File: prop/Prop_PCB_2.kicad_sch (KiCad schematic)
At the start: 42 parts

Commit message: finalize3pcb schematic
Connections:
- net CS is gone; now on net CS1: U?.10 (~{CS}/SHDN)
- net aData0: now also J?.3
- net aData1: now also J?.3
- net aData2: now also J?.3
- net aData3: now also J?.3
- net aData4: now also J?.3
- no-connect marks 31 -> 38

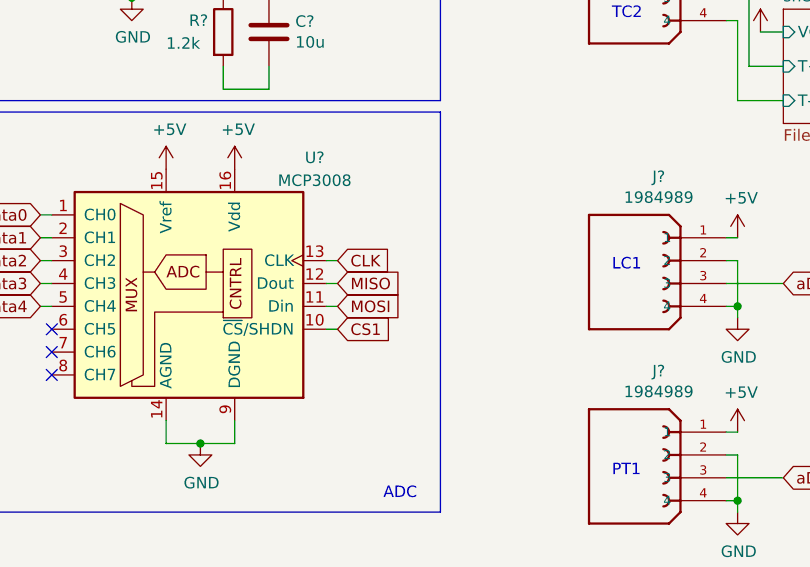
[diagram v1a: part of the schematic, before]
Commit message: fix spelling errors in signals
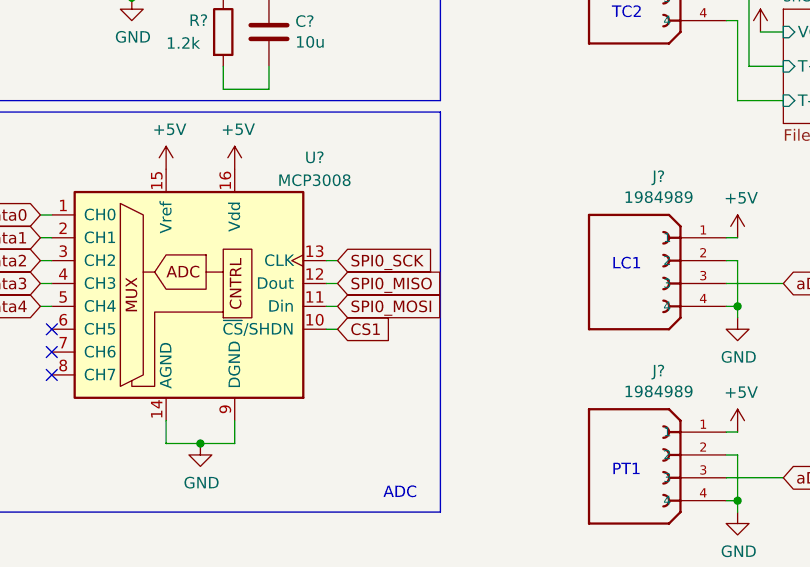
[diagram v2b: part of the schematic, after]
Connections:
- net CLK is gone; now on net SPI0_SCK: U?.13 (CLK)
- net MISO is gone; now on net SPI0_MISO: U?.12 (Dout)
- net MOSI is gone; now on net SPI0_MOSI: U?.11 (Din)
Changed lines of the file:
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@@
     (effects (font (size 1.27 1.27)) (justify left bottom))
   )
-  (global_label "MISO" (shape input) (at 113.03 74.93 0) (fields_autoplaced)
+  (global_label "SPI0_MISO" (shape input) (at 113.03 74.93 0) (fields_autoplaced)
     (effects (font (size 1.27 1.27)) (justify left))
-    (property "Intersheet References" "${INTERSHEET_REFS}" (id 0) (at 120.0393 74.8506 0)
+    (property "Intersheet References" "${INTERSHEET_REFS}" (id 0) (at 125.3007 74.8506 0)
       (effects (font (size 1.27 1.27)) (justify left) hide)
     )
@@
     )
   )
-  (global_label "CLK" (shape input) (at 113.03 72.39 0) (fields_autoplaced)
+  (global_label "SPI0_SCK" (shape input) (at 113.03 72.39 0) (fields_autoplaced)
     (effects (font (size 1.27 1.27)) (justify left))
-    (property "Intersheet References" "${INTERSHEET_REFS}" (id 0) (at 119.0112 72.3106 0)
+    (property "Intersheet References" "${INTERSHEET_REFS}" (id 0) (at 124.4541 72.3106 0)
       (effects (font (size 1.27 1.27)) (justify left) hide)
     )
@@
     )
   )
-  (global_label "MOSI" (shape input) (at 113.03 77.47 0) (fields_autoplaced)
+  (global_label "SPI0_MOSI" (shape input) (at 113.03 77.47 0) (fields_autoplaced)
     (effects (font (size 1.27 1.27)) (justify left))
-    (property "Intersheet References" "${INTERSHEET_REFS}" (id 0) (at 120.0393 77.3906 0)
+    (property "Intersheet References" "${INTERSHEET_REFS}" (id 0) (at 125.3007 77.3906 0)
       (effects (font (size 1.27 1.27)) (justify left) hide)
     )
@@
       (reference "#PWR?") (unit 1) (value "GND") (footprint "")
     )
+    (path "/49575217-40b0-4890-8acf-12982cca52b5/00000000-0000-0000-0000-000060597f92"
+      (reference "#PWR?") (unit 1) (value "GND") (footprint "")
+    )
     (path "/7db990e4-92e1-4f99-b4d2-435bbec1ba83/00000000-0000-0000-0000-000060597f92"
-      (reference "#PWR?") (unit 1) (value "GND") (footprint "")
-    )
-    (path "/49575217-40b0-4890-8acf-12982cca52b5/00000000-0000-0000-0000-000060597f92"
       (reference "#PWR?") (unit 1) (value "GND") (footprint "")
     )
@@
       (reference "U?") (unit 1) (value "MCP3008") (footprint "Package_SO:SOIC-16_3.9x9.9mm_P1.27mm")
     )
+    (path "/49575217-40b0-4890-8acf-12982cca52b5/65a8b55e-a85b-43de-a7c0-277e3d0e143e"
+      (reference "U?") (unit 1) (value "MAX6675ISA+") (footprint "star-common-lib:SOIC127P600X175-8N")
+    )
     (path "/7db990e4-92e1-4f99-b4d2-435bbec1ba83/65a8b55e-a85b-43de-a7c0-277e3d0e143e"
       (reference "U?") (unit 1) (value "MAX6675ISA+") (footprint "star-common-lib:SOIC127P600X175-8N")
     )
-    (path "/49575217-40b0-4890-8acf-12982cca52b5/65a8b55e-a85b-43de-a7c0-277e3d0e143e"
-      (reference "U?") (unit 1) (value "MAX6675ISA+") (footprint "star-common-lib:SOIC127P600X175-8N")
-    )

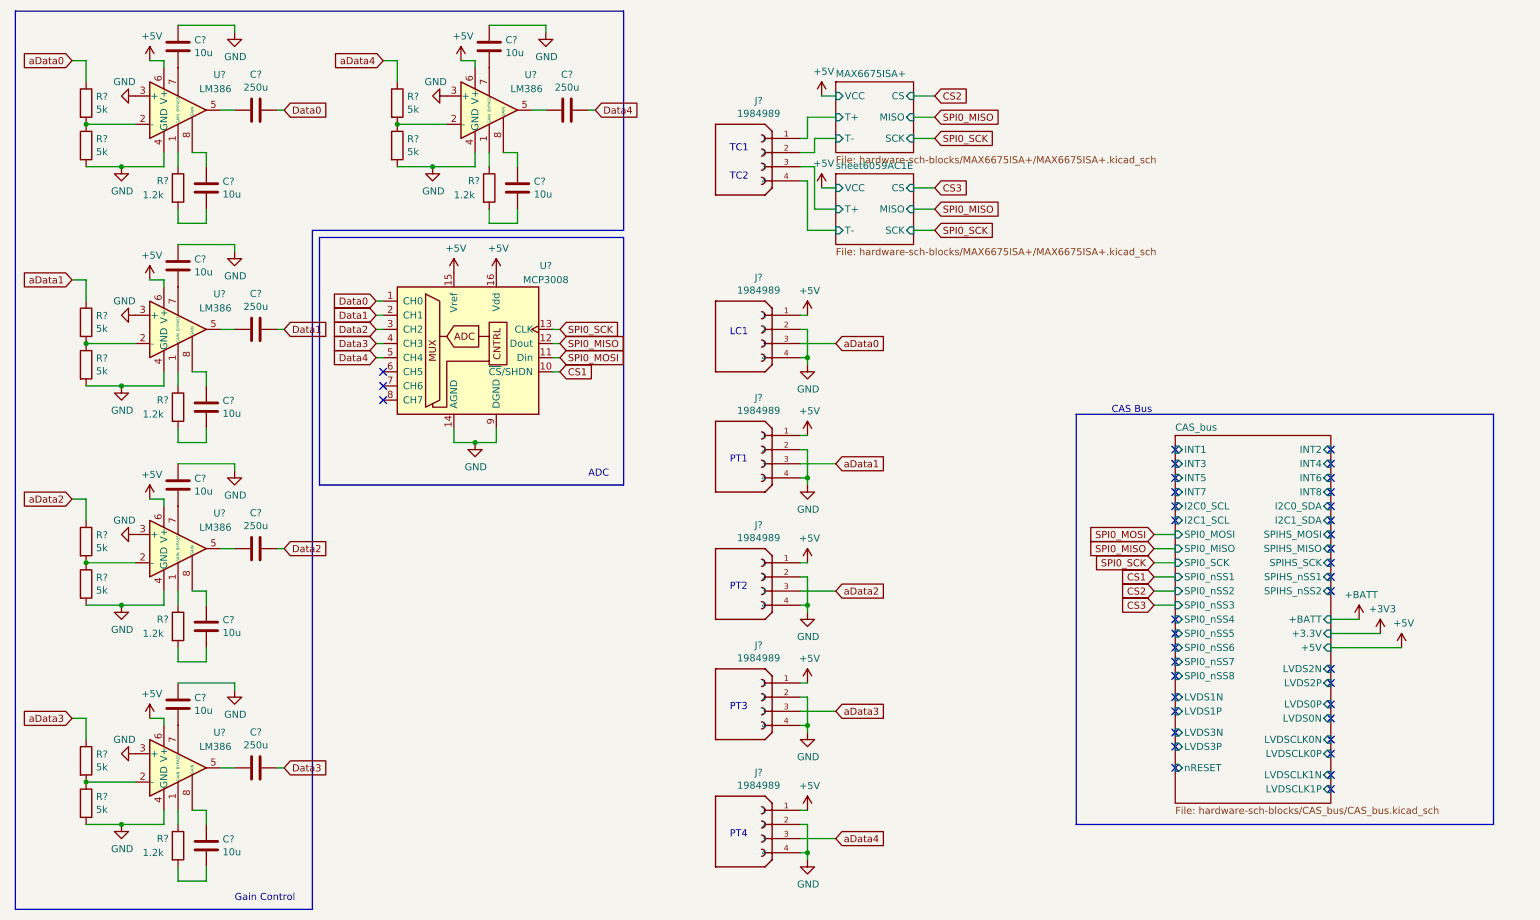
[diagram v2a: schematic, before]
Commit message: rearranged the pcb to be more neat
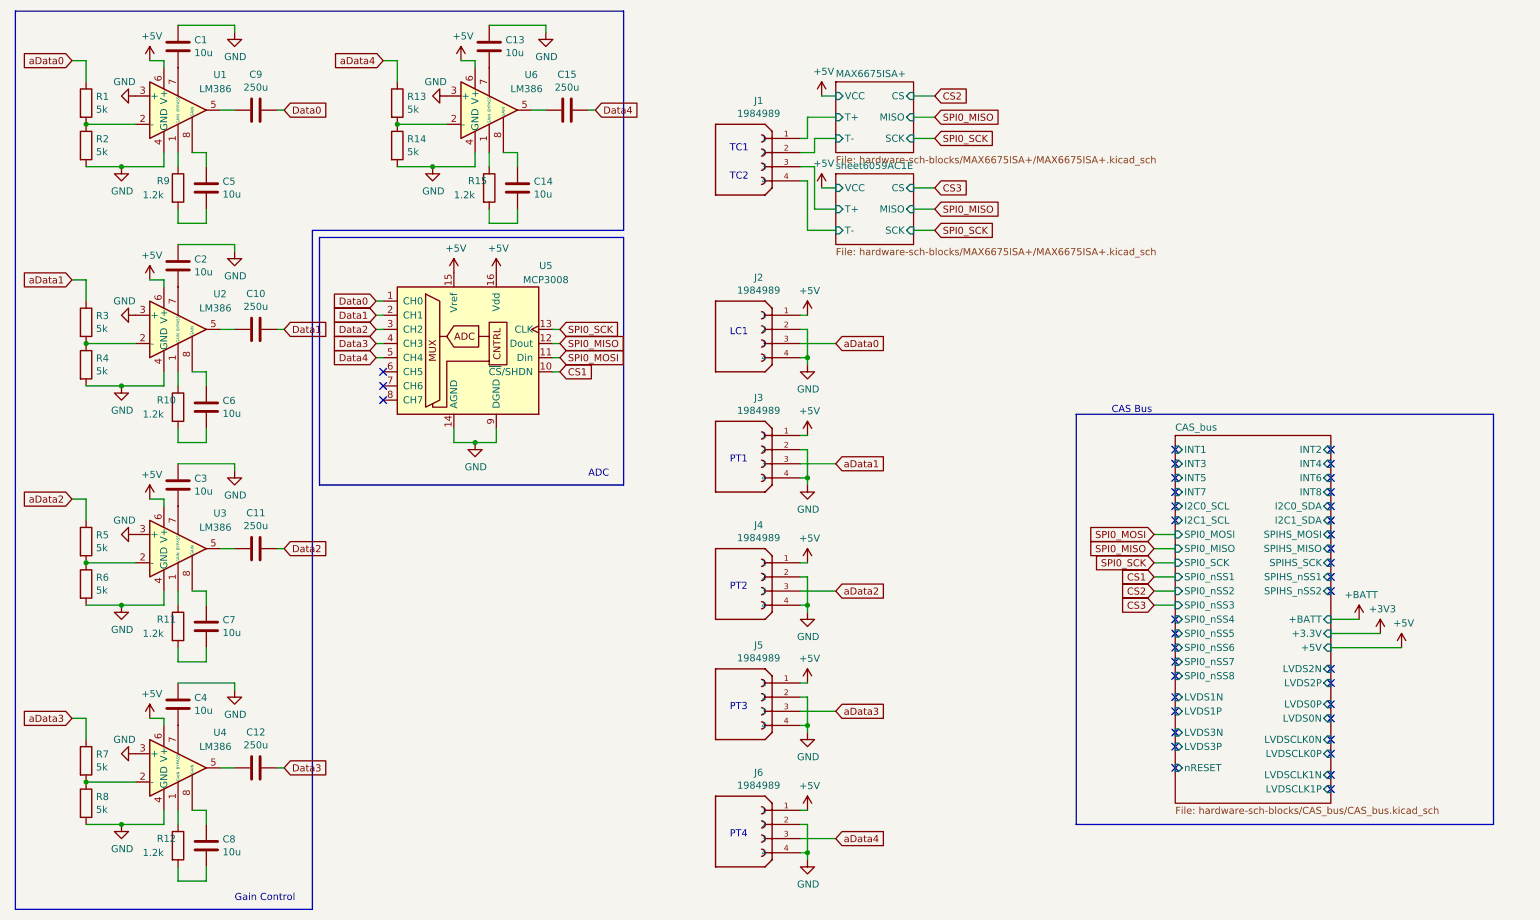
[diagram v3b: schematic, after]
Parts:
- gave numbers to parts that had none: 42
